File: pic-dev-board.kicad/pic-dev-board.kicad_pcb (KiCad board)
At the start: 2 copper layers, 100 x 100 mm, 74 parts, among them J1 Conn_GP0, J10 Jumper DATin, J11 Conn_SR_2, J12 Conn_SR_1, J13 Conn_5V_GND, J14 Jumper CLKin, J15 Barrel_Jack_Switch, J16 RUN/~PGM, J17 I2C, J18 GP1(RA1)/RB6, J19 GP2(RA2)/RB4, J2 Conn_GP4, J3 Conn_GP1, J4 Conn_GP5, J5 Conn_GP2, J6 Conn_ICSP, J7 Conn_TRISC, J8 Conn_TRISA, J9 Conn_TRISB, SW1 SW_Push, U1 PIC16F690-IP, U2 74HC595, U3 74HC595

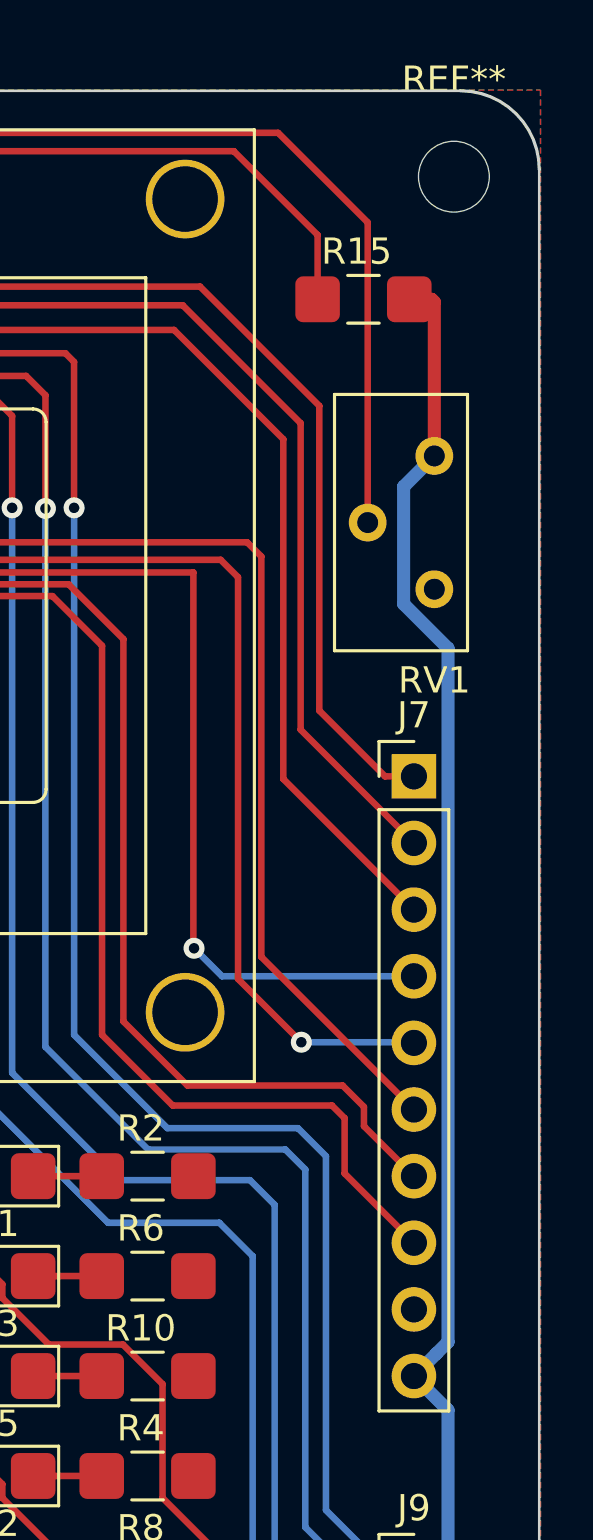
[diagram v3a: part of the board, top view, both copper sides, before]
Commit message: fixed footprint for poti
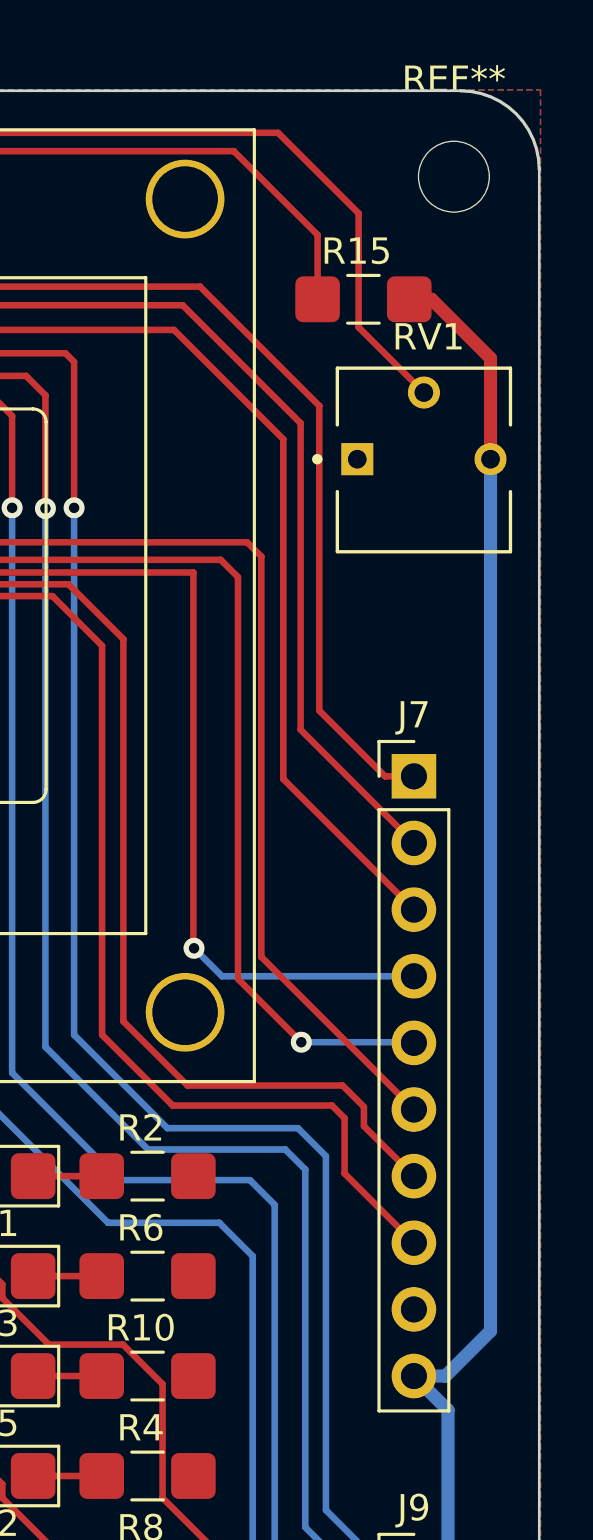
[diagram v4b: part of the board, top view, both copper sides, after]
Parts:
- RV1: footprint Potentiometer_THT:Potentiometer_Bourns_3386X_Horizontal -> user:TRIM_3362P-1-103
- moved RV1 4.97 mm to (125.6, 44.0), turned to 0 degrees
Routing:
- net Net-(DS1-Pad3): track 86.2 -> 82.1 mm
- net +5V: track 358.4 -> 359.4 mm
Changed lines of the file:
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@@
     (thickness 1.6)
     (drawings 8)
-    (tracks 649)
+    (tracks 648)
     (zones 0)
     (modules 74)
@@
     (add_net /Vdd)
   )
+  (module user:TRIM_3362P-1-103 (layer F.Cu)
+    (at 125.603 44.0436)
+    (fp_text reference RV1 (at 0.17547 -4.64779) (layer F.SilkS)
+      (effects (font (size 1.002756 1.002756) (thickness 0.015)))
+    )
+    (fp_text value 10K (at 6.7769 4.67565) (layer F.Fab)
+      (effects (font (size 1.002394 1.002394) (thickness 0.015)))
+    )
+    (fp_circle (center -4.064 0) (end -3.964 0) (layer F.SilkS) (width 0.2))
+    (fp_line (start 3.3 3.53) (end -3.3 3.53) (layer F.SilkS) (width 0.127))
+    (fp_line (start -3.3 3.53) (end -3.3 -3.47) (layer F.Fab) (width 0.127))
+    (fp_line (start 3.3 3.53) (end -3.3 3.53) (layer F.Fab) (width 0.127))
+    (fp_line (start 3.3 -3.47) (end 3.3 3.53) (layer F.Fab) (width 0.127))
+    (fp_line (start -3.3 -3.47) (end 3.3 -3.47) (layer F.Fab) (width 0.127))
+    (fp_line (start 3.55 -3.72) (end 3.55 3.78) (layer F.CrtYd) (width 0.05))
+    (fp_line (start -3.55 -3.72) (end 3.55 -3.72) (layer F.CrtYd) (width 0.05))
+    (fp_line (start -3.55 3.78) (end -3.55 -3.72) (layer F.CrtYd) (width 0.05))
+    (fp_line (start 3.55 3.78) (end -3.55 3.78) (layer F.CrtYd) (width 0.05))
+    (fp_line (start 3.3 1.235) (end 3.3 3.52) (layer F.SilkS) (width 0.127))
+    (fp_line (start 3.3 -3.47) (end 3.3 -1.305) (layer F.SilkS) (width 0.127))
+    (fp_line (start -3.3 -3.47) (end 3.3 -3.47) (layer F.SilkS) (width 0.127))
+    (fp_line (start -3.3 -1.305) (end -3.3 -3.47) (layer F.SilkS) (width 0.127))
+    (fp_line (start -3.3 3.52) (end -3.3 1.235) (layer F.SilkS) (width 0.127))
+    (pad 1 thru_hole rect (at -2.54 0) (size 1.222 1.222) (drill 0.714) (layers *.Cu *.Mask)
+      (net 2 GND))
+    (pad 2 thru_hole circle (at 0 -2.54) (size 1.222 1.222) (drill 0.714) (layers *.Cu *.Mask)
+      (net 52 "Net-(DS1-Pad3)"))
+    (pad 3 thru_hole circle (at 2.54 0) (size 1.222 1.222) (drill 0.714) (layers *.Cu *.Mask)
+      (net 53 +5V))
+  )
   (module user:WC1602A_Connector (layer F.Cu)
     (at 47 34.1276)
@@
     )
   )
-  (module Potentiometer_THT:Potentiometer_Bourns_3386X_Horizontal (layer F.Cu)
-    (at 126 49 180)
-    (descr "Potentiometer, horizontal, Bourns 3386X, https://www.bourns.com/pdfs/3386.pdf")
-    (tags "Potentiometer horizontal Bourns 3386X")
-    (fp_text reference RV1 (at 0 -3.475) (layer F.SilkS)
-      (effects (font (size 1 1) (thickness 0.15)))
-    )
-    (fp_text value 10K (at 0 8.555) (layer F.Fab)
-      (effects (font (size 1 1) (thickness 0.15)))
-    )
-    (fp_text user %R (at 1.27 2.54) (layer F.Fab)
-      (effects (font (size 1 1) (thickness 0.15)))
-    )
-    (fp_line (start 3.94 -2.48) (end -1.4 -2.48) (layer F.CrtYd) (width 0.05))
-    (fp_line (start 3.94 7.56) (end 3.94 -2.48) (layer F.CrtYd) (width 0.05))
-    (fp_line (start -1.4 7.56) (end 3.94 7.56) (layer F.CrtYd) (width 0.05))
-    (fp_line (start -1.4 -2.48) (end -1.4 7.56) (layer F.CrtYd) (width 0.05))
-    (fp_line (start -1.265 -2.345) (end -1.265 7.425) (layer F.SilkS) (width 0.12))
-    (fp_line (start 3.805 -2.345) (end 3.805 7.425) (layer F.SilkS) (width 0.12))
-    (fp_line (start -1.265 7.425) (end 3.805 7.425) (layer F.SilkS) (width 0.12))
-    (fp_line (start -1.265 -2.345) (end 3.805 -2.345) (layer F.SilkS) (width 0.12))
-    (fp_line (start -1.145 -2.225) (end 3.685 -2.225) (layer F.Fab) (width 0.1))
-    (fp_line (start -1.145 7.305) (end -1.145 -2.225) (layer F.Fab) (width 0.1))
-    (fp_line (start 3.685 7.305) (end -1.145 7.305) (layer F.Fab) (width 0.1))
-    (fp_line (start 3.685 -2.225) (end 3.685 7.305) (layer F.Fab) (width 0.1))
-    (pad 1 thru_hole circle (at 0 0 180) (size 1.44 1.44) (drill 0.8) (layers *.Cu *.Mask)
-      (net 2 GND))
-    (pad 2 thru_hole circle (at 2.54 2.54 180) (size 1.44 1.44) (drill 0.8) (layers *.Cu *.Mask)
-      (net 52 "Net-(DS1-Pad3)"))
-    (pad 3 thru_hole circle (at 0 5.08 180) (size 1.44 1.44) (drill 0.8) (layers *.Cu *.Mask)
-      (net 53 +5V))
-    (model ${KISYS3DMOD}/Potentiometer_THT.3dshapes/Potentiometer_Bourns_3386X_Horizontal.wrl
-      (at (xyz 0 0 0))
-      (scale (xyz 1 1 1))
-      (rotate (xyz 0 0 0))
-    )
-  )
   (module Resistor_THT:R_Array_SIP9 (layer F.Cu)
     (at 68.326 64.77 180)
@@
   (segment (start 122.174 89.962136) (end 122.174 101.938) (width 0.25) (layer F.Cu) (net 51))
   (segment (start 122.174 101.938) (end 124.122 103.886) (width 0.25) (layer F.Cu) (net 51))
-  (segment (start 53.055011 31.602589) (end 52.08 32.5776) (width 0.25) (layer F.Cu) (net 52))
-  (segment (start 52.08 32.5776) (end 52.08 34.1276) (width 0.25) (layer F.Cu) (net 52))
   (segment (start 120.045389 31.602589) (end 53.055011 31.602589) (width 0.25) (layer F.Cu) (net 52))
-  (segment (start 123.46 46.46) (end 123.46 35.0172) (width 0.25) (layer F.Cu) (net 52))
-  (segment (start 123.46 35.0172) (end 120.045389 31.602589) (width 0.25) (layer F.Cu) (net 52))
+  (segment (start 52.08 32.5776) (end 52.08 34.1276) (width 0.25) (layer F.Cu) (net 52))
+  (segment (start 53.055011 31.602589) (end 52.08 32.5776) (width 0.25) (layer F.Cu) (net 52))
+  (segment (start 125.603 41.5036) (end 123.1138 39.0144) (width 0.25) (layer F.Cu) (net 52))
+  (segment (start 123.1138 34.671) (end 120.045389 31.602589) (width 0.25) (layer F.Cu) (net 52))
+  (segment (start 123.1138 39.0144) (end 123.1138 34.671) (width 0.25) (layer F.Cu) (net 52))
   (segment (start 49.295999 85.070001) (end 49.746001 84.619999) (width 0.5) (layer B.Cu) (net 53))
   (segment (start 48.387997 85.070001) (end 49.295999 85.070001) (width 0.5) (layer B.Cu) (net 53))
@@
   (segment (start 65.786 83.82) (end 69.342 87.122) (width 0.5) (layer F.Cu) (net 53))
   (segment (start 69.342 87.122) (end 71.12 89.408) (width 0.5) (layer F.Cu) (net 53))
-  (segment (start 126.071999 78.144001) (end 125.222 78.994) (width 0.5) (layer B.Cu) (net 53))
-  (segment (start 126.522001 77.693999) (end 126.071999 78.144001) (width 0.5) (layer B.Cu) (net 53))
-  (segment (start 124.829999 49.561601) (end 126.522001 51.253603) (width 0.5) (layer B.Cu) (net 53))
-  (segment (start 124.829999 45.090001) (end 124.829999 49.561601) (width 0.5) (layer B.Cu) (net 53))
-  (segment (start 126.522001 51.253603) (end 126.522001 77.693999) (width 0.5) (layer B.Cu) (net 53))
-  (segment (start 126 43.92) (end 124.829999 45.090001) (width 0.5) (layer B.Cu) (net 53))
   (segment (start 126.522001 97.759999) (end 126.071999 98.210001) (width 0.5) (layer B.Cu) (net 53))
   (segment (start 126.522001 80.294001) (end 126.522001 97.759999) (width 0.5) (layer B.Cu) (net 53))
@@
   (segment (start 37.451 72.6195) (end 36.576 72.6195) (width 0.5) (layer F.Cu) (net 53))
   (segment (start 44 79.1685) (end 37.451 72.6195) (width 0.5) (layer F.Cu) (net 53))
-  (segment (start 126 38.0525) (end 125.8951 37.9476) (width 0.5) (layer F.Cu) (net 53))
+  (segment (start 126.424081 78.994) (end 128.143 77.275081) (width 0.5) (layer B.Cu) (net 53))
+  (segment (start 128.143 44.907684) (end 128.143 44.0436) (width 0.5) (layer B.Cu) (net 53))
+  (segment (start 128.143 77.275081) (end 128.143 44.907684) (width 0.5) (layer B.Cu) (net 53))
+  (segment (start 125.222 78.994) (end 126.424081 78.994) (width 0.5) (layer B.Cu) (net 53))
   (segment (start 125.8951 37.9476) (end 125.0451 37.9476) (width 0.5) (layer F.Cu) (net 53))
-  (segment (start 126 43.92) (end 126 38.0525) (width 0.5) (layer F.Cu) (net 53))
+  (segment (start 128.143 40.1955) (end 125.8951 37.9476) (width 0.5) (layer F.Cu) (net 53))
+  (segment (start 128.143 44.0436) (end 128.143 40.1955) (width 0.5) (layer F.Cu) (net 53))
   (segment (start 98.468 71.374) (end 96.4955 71.374) (width 0.25) (layer F.Cu) (net 54))
   (segment (start 99.568 71.374) (end 98.468 71.374) (width 0.25) (layer F.Cu) (net 54))

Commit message: updated footprint for +5V/GND connector
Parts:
- J13: footprint Connector_PinHeader_2.54mm:PinHeader_2x15_P2.54mm_Vertical -> user:PinHeader_2x15_P2.54mm_Vertical_Slim

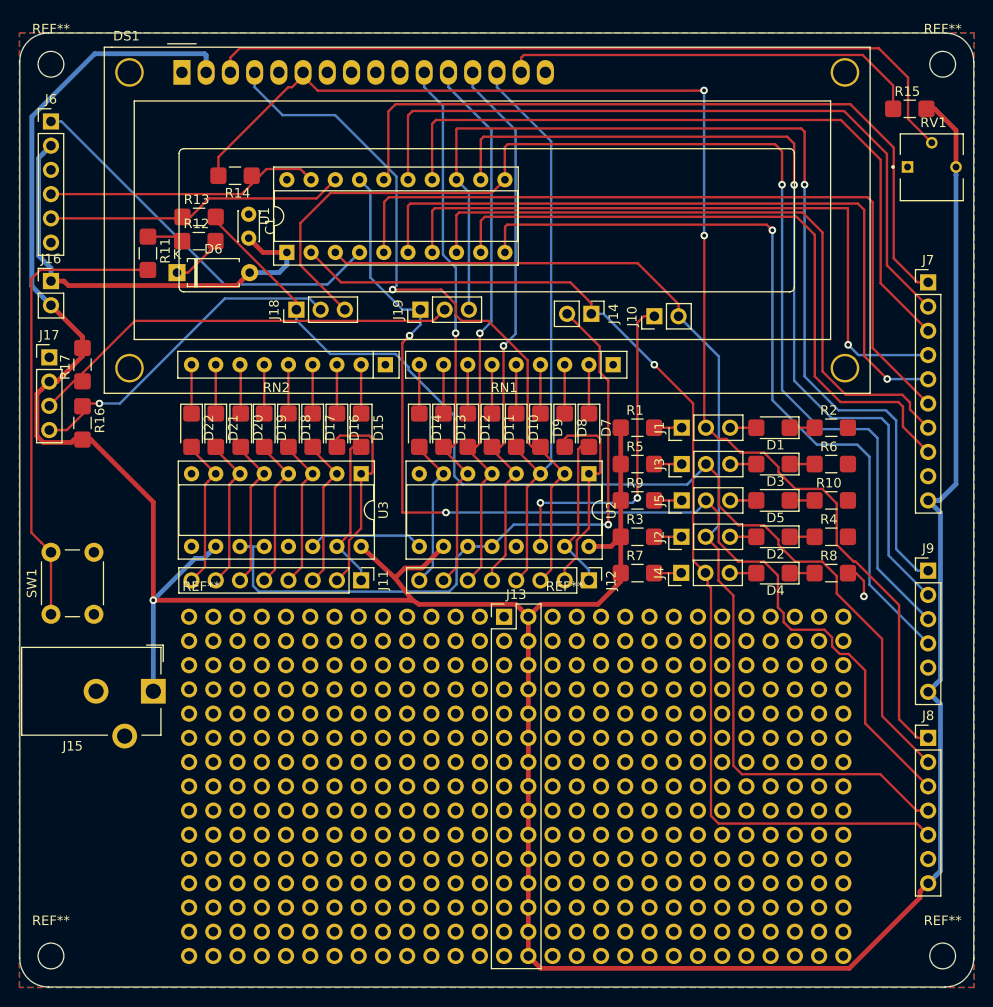
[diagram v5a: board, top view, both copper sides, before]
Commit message: moved reset button and power-connector
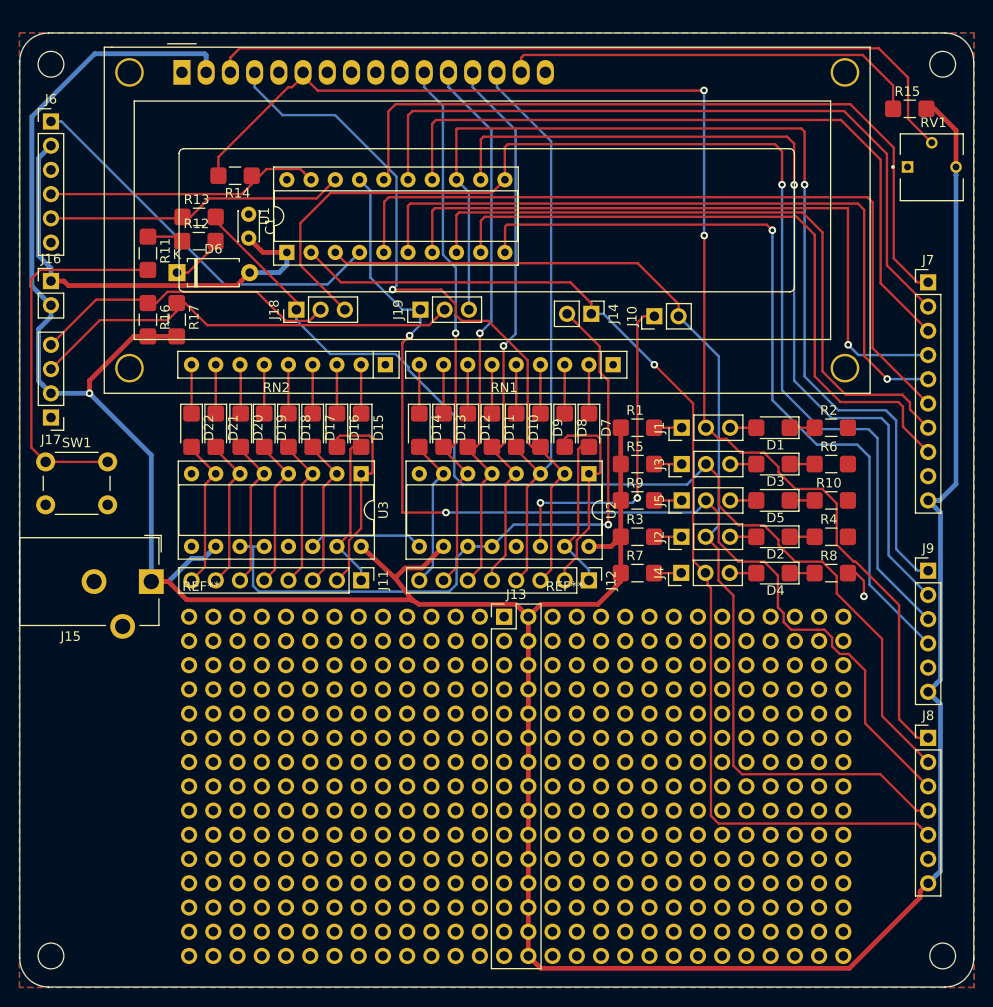
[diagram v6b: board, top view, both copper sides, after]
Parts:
- moved SW1 16.0 mm to (32.7, 75.0), turned to 0 degrees
- moved R16 12.8 mm to (43.4, 59.8)
- moved J15 11.5 mm to (43.8, 87.5)
- moved R17 11.2 mm to (46.5, 59.8), turned to 270 degrees
- moved J17 6.31 mm to (33.3, 70.3), turned to 180 degrees
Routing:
- net Net-(R11-Pad2): track 48.6 -> 38.9 mm
- net /SCL: track 35.1 -> 32.3 mm, vias 1 -> 0
- net +5V: track 359.4 -> 356.6 mm
- net /SDA: track 46.1 -> 47.1 mm
